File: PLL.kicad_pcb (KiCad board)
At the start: 2 copper layers, 8 parts, among them Q1 BC557, Q2 BC547, U1 74HC74, U2 7400

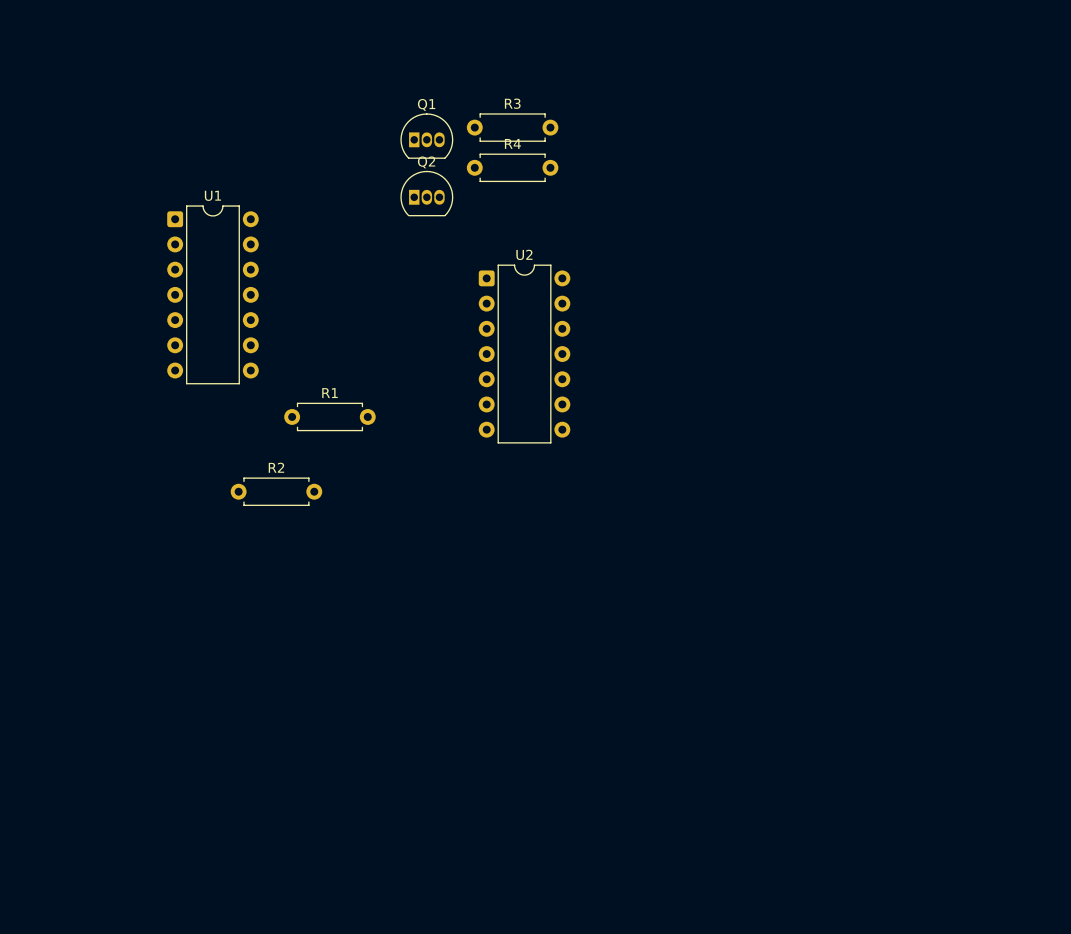
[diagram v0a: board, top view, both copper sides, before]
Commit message: Added Low-Pass Filter and footprints for resistors
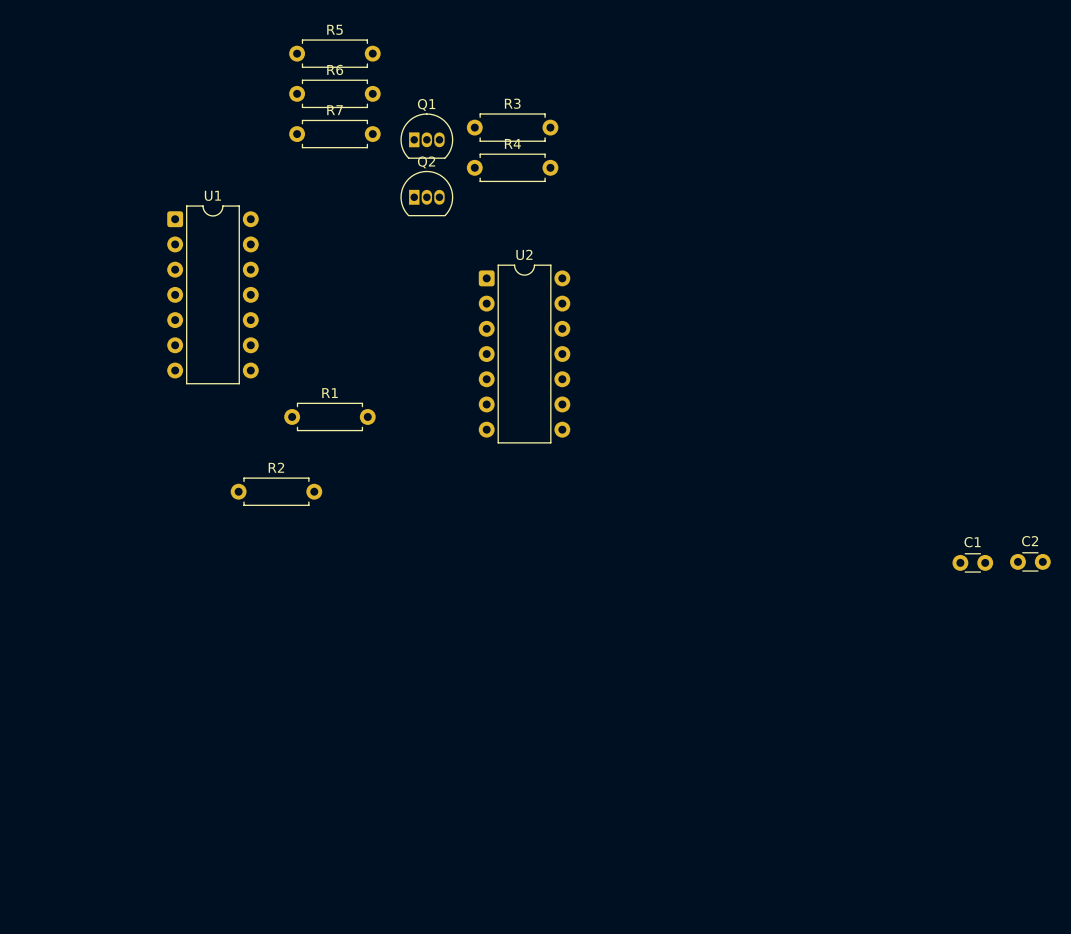
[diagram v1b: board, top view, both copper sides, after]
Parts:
- added C1: 68nF, Capacitor_THT:C_Disc_D3.0mm_W1.6mm_P2.50mm, F.Cu at (136.6, 85.2)
- added C2: 10nf, Capacitor_THT:C_Disc_D3.0mm_W1.6mm_P2.50mm, F.Cu at (142.4, 85.1)
- added R5: 47k, Resistor_THT:R_Axial_DIN0207_L6.3mm_D2.5mm_P7.62mm_Horizontal, F.Cu at (69.8, 33.9)
- added R6: 47k, Resistor_THT:R_Axial_DIN0207_L6.3mm_D2.5mm_P7.62mm_Horizontal, F.Cu at (69.8, 38.0)
- added R7: 33k, Resistor_THT:R_Axial_DIN0207_L6.3mm_D2.5mm_P7.62mm_Horizontal, F.Cu at (69.8, 42.0)

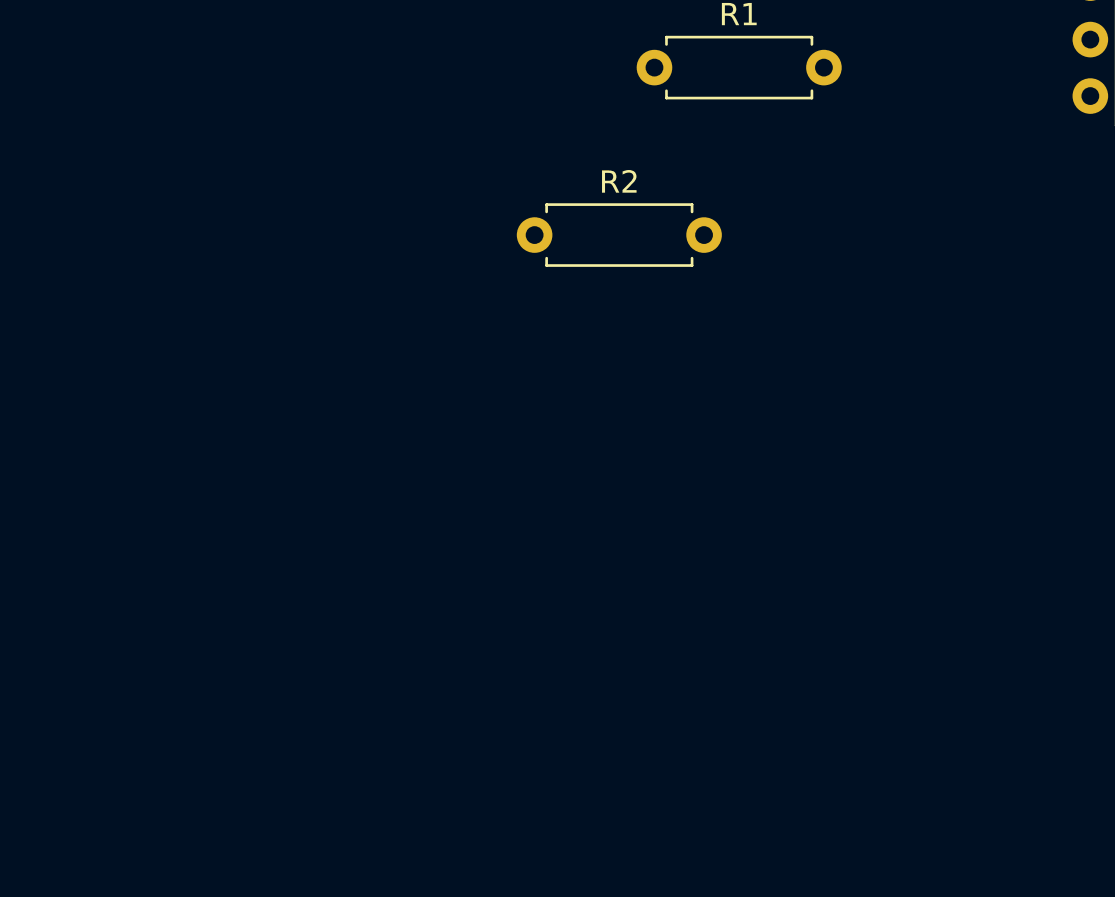
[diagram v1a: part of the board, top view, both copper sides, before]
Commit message: 555 Timer Voltage controlled oscillator circuitry added
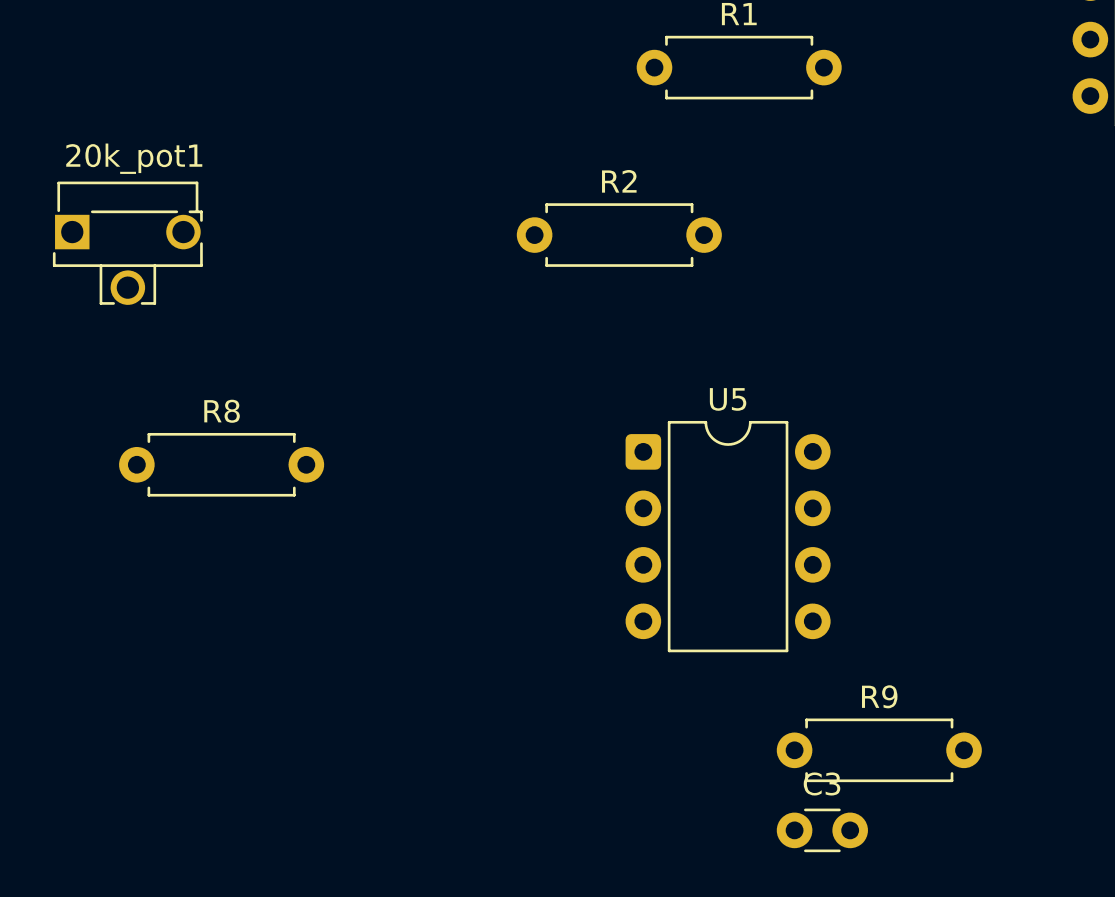
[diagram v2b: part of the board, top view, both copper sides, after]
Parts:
- added 20k_pot1: R_Potentiometer_Trim, Potentiometer_THT:Potentiometer_Runtron_RM-063_Horizontal, F.Cu at (43.1, 77.9)
- added C3: 10nf, Capacitor_THT:C_Disc_D3.0mm_W1.6mm_P2.50mm, F.Cu at (75.6, 104.8)
- added R8: 10k, Resistor_THT:R_Axial_DIN0207_L6.3mm_D2.5mm_P7.62mm_Horizontal, F.Cu at (46.0, 88.4)
- added R9: 15k, Resistor_THT:R_Axial_DIN0207_L6.3mm_D2.5mm_P7.62mm_Horizontal, F.Cu at (75.6, 101.2)
- added U5: NE555P, Package_DIP:DIP-8_W7.62mm, F.Cu at (68.8, 87.8)
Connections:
- U1 pad 11: unconnected-(U1B-C-Pad11) -> /f_fb
- U1 pad 3: unconnected-(U1A-C-Pad3) -> /f_ref

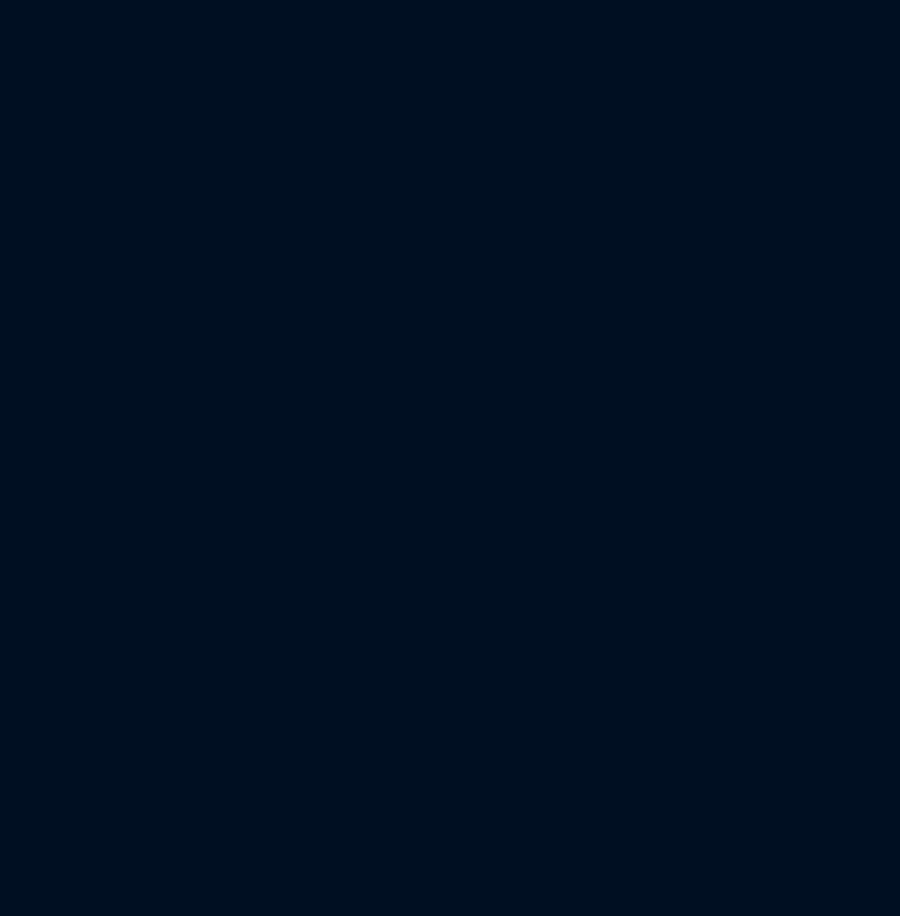
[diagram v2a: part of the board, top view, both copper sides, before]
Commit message: Divide by 4 counter added
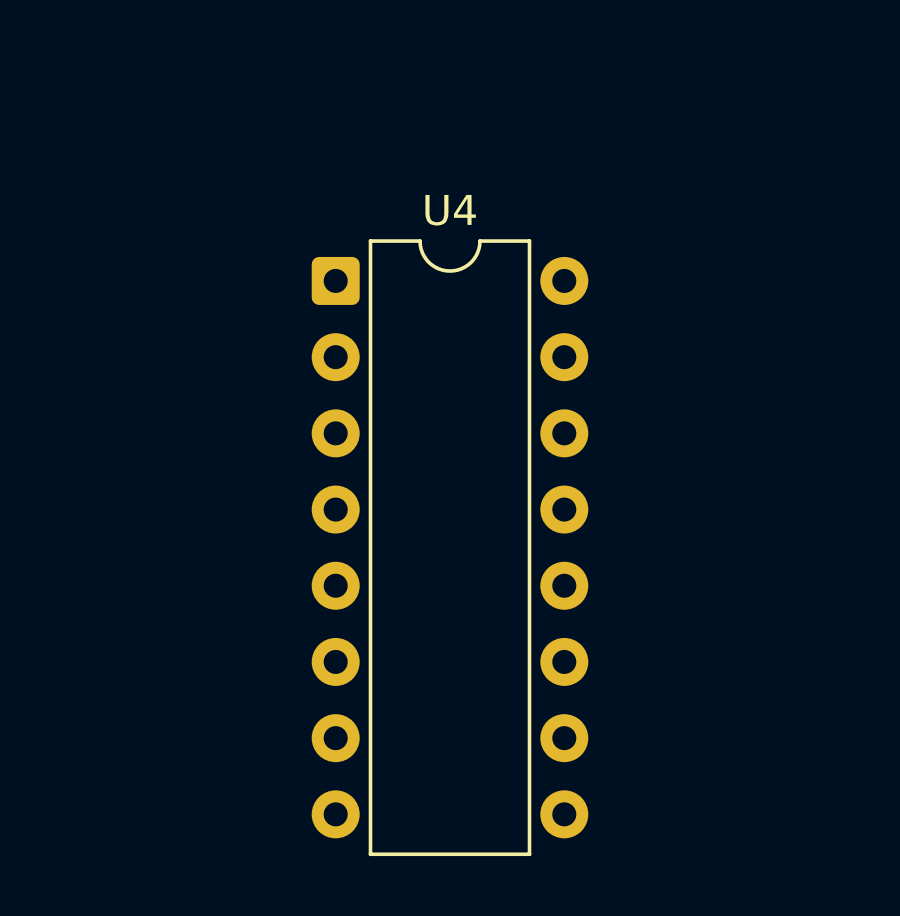
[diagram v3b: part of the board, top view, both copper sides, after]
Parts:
- added U4: 4040, Package_DIP:DIP-16_W7.62mm, F.Cu at (114.5, 101.4)
